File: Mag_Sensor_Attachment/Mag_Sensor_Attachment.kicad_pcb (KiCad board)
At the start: 2 copper layers, 14 x 15.8 mm, 5 parts, among them J2 Conn_01x06_Socket, U1 MA730

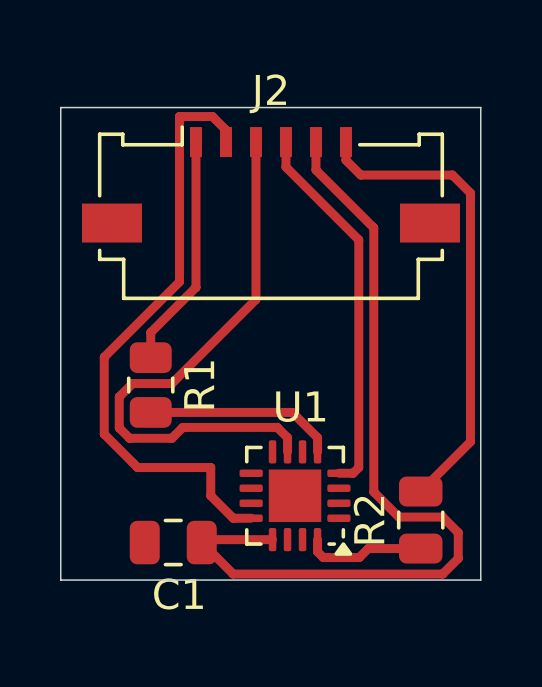
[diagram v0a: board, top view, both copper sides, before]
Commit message: added to schematic
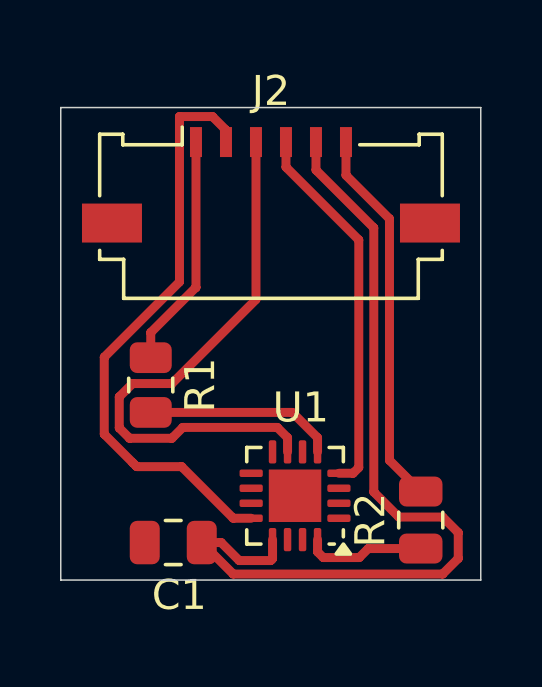
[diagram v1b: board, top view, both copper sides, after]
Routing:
- net /Mag_High: track 15.8 -> 12.7 mm
- net /VDD: track 28.3 -> 29.2 mm
- net /MAG_CLK: track 20.4 -> 19.8 mm
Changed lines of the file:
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@@
 	)
 	(segment
-		(start 149.56 99.4025)
-		(end 147.2975 99.4025)
+		(start 147.8475 99.5)
+		(end 147.2 99.5)
 		(width 0.3)
 		(layer "F.Cu")
@@
 	)
 	(segment
+		(start 149.56 99.4025)
+		(end 149.56 100.04)
+		(width 0.3)
+		(layer "F.Cu")
+		(net 2)
+	)
+	(segment
 		(start 152.934772 89.009772)
 		(end 152.934772 97.815228)
@@
 	)
 	(segment
+		(start 149.5 100.1)
+		(end 148.4475 100.1)
+		(width 0.3)
+		(layer "F.Cu")
+		(net 2)
+	)
+	(segment
+		(start 149.56 100.04)
+		(end 149.5 100.1)
+		(width 0.3)
+		(layer "F.Cu")
+		(net 2)
+	)
+	(segment
 		(start 148.25 100.55)
 		(end 147.2 99.5)
@@
 	)
 	(segment
-		(start 147.2975 99.4025)
-		(end 147.2 99.5)
+		(start 148.4475 100.1)
+		(end 147.8475 99.5)
 		(width 0.3)
 		(layer "F.Cu")
@@
 	)
 	(segment
+		(start 146.4575 90.812044)
+		(end 146.4575 85.3)
+		(width 0.3)
+		(layer "F.Cu")
+		(net 6)
+	)
+	(segment
+		(start 145.031218 96.968782)
+		(end 144.906218 96.843782)
+		(width 0.3)
+		(layer "F.Cu")
+		(net 6)
+	)
+	(segment
+		(start 143.95 93.319544)
+		(end 146.4575 90.812044)
+		(width 0.3)
+		(layer "F.Cu")
+		(net 6)
+	)
+	(segment
+		(start 148.25 98.69)
+		(end 146.528782 96.968782)
+		(width 0.3)
+		(layer "F.Cu")
+		(net 6)
+	)
+	(segment
+		(start 144.906218 96.843782)
+		(end 143.95 95.887563)
+		(width 0.3)
+		(layer "F.Cu")
+		(net 6)
+	)
+	(segment
+		(start 147.5575 85.3)
+		(end 148.0075 85.75)
+		(width 0.3)
+		(layer "F.Cu")
+		(net 6)
+	)
+	(segment
+		(start 148.0075 85.75)
+		(end 148.0075 86.15)
+		(width 0.3)
+		(layer "F.Cu")
+		(net 6)
+	)
+	(segment
+		(start 146.528782 96.968782)
+		(end 145.031218 96.968782)
+		(width 0.3)
+		(layer "F.Cu")
+		(net 6)
+	)
+	(segment
 		(start 143.95 95.887563)
-		(end 144.906218 96.843782)
-		(width 0.3)
-		(layer "F.Cu")
-		(net 6)
-	)
-	(segment
-		(start 148.0075 86.15)
-		(end 148.0075 85.75)
-		(width 0.3)
-		(layer "F.Cu")
-		(net 6)
-	)
-	(segment
-		(start 147.5575 85.3)
-		(end 146.4575 85.3)
-		(width 0.3)
-		(layer "F.Cu")
-		(net 6)
-	)
-	(segment
-		(start 143.95 93.319544)
-		(end 143.95 95.887563)
-		(width 0.3)
-		(layer "F.Cu")
-		(net 6)
-	)
-	(segment
-		(start 148.25 98.69)
-		(end 147.5 97.94)
-		(width 0.3)
-		(layer "F.Cu")
-		(net 6)
-	)
-	(segment
-		(start 146.4575 90.812044)
 		(end 143.95 93.319544)
 		(width 0.3)
@@
 	(segment
 		(start 146.4575 85.3)
-		(end 146.4575 90.812044)
-		(width 0.3)
-		(layer "F.Cu")
-		(net 6)
-	)
-	(segment
-		(start 148.0075 85.75)
 		(end 147.5575 85.3)
 		(width 0.3)
@@
 	)
 	(segment
-		(start 147.5 97)
-		(end 145.062436 97)
-		(width 0.3)
-		(layer "F.Cu")
-		(net 6)
-	)
-	(segment
-		(start 148.25 98.69)
-		(end 148.8475 98.69)
-		(width 0.3)
-		(layer "F.Cu")
-		(net 6)
-	)
-	(segment
-		(start 147.5 97.94)
-		(end 147.5 97)
-		(width 0.3)
-		(layer "F.Cu")
-		(net 6)
-	)
-	(segment
-		(start 145.062436 97)
-		(end 144.906218 96.843782)
-		(width 0.3)
-		(layer "F.Cu")
-		(net 6)
-	)
-	(segment
-		(start 156.1575 87.85)
-		(end 156.1575 96.1425)
+		(start 148.8475 98.69)
+		(end 148.25 98.69)
+		(width 0.3)
+		(layer "F.Cu")
+		(net 6)
+	)
+	(segment
+		(start 152.0075 87.2575)
+		(end 152.0075 86.15)
 		(width 0.3)
 		(layer "F.Cu")
@@
 	)
 	(segment
-		(start 156.1575 96.1425)
-		(end 154.5 97.8)
+		(start 153.4575 88.7075)
+		(end 152.0075 87.2575)
 		(width 0.3)
 		(layer "F.Cu")
@@
 	)
 	(segment
-		(start 155.5575 87.25)
-		(end 156.1575 87.85)
+		(start 153.4575 96.7575)
+		(end 153.4575 88.7075)
 		(width 0.3)
 		(layer "F.Cu")
@@
 	)
 	(segment
-		(start 152.5 87.25)
-		(end 155.5575 87.25)
-		(width 0.3)
-		(layer "F.Cu")
-		(net 7)
-	)
-	(segment
-		(start 152.0075 86.15)
-		(end 152.0075 86.7575)
-		(width 0.3)
-		(layer "F.Cu")
-		(net 7)
-	)
-	(segment
-		(start 152.0075 86.7575)
-		(end 152.5 87.25)
-		(width 0.3)
-		(layer "F.Cu")
+		(start 154.5 97.8)
+		(end 153.4575 96.7575)
+		(width 0.3)
+		(layer "F.Cu")

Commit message: Check up
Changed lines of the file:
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@@
 		(start 152.434772 89.412272)
 		(end 150.0075 86.985)
-		(width 0.3)
+		(width 0.15)
 		(layer "F.Cu")
 		(net 3)
@@
 		(start 152.244772 97.19)
 		(end 152.434772 97)
-		(width 0.3)
+		(width 0.15)
 		(layer "F.Cu")
 		(net 3)
@@
 		(start 150.0075 86.985)
 		(end 150.0075 86.15)
-		(width 0.3)
+		(width 0.15)
 		(layer "F.Cu")
 		(net 3)
@@
 		(start 151.7725 97.19)
 		(end 152.244772 97.19)
-		(width 0.3)
+		(width 0.15)
 		(layer "F.Cu")
 		(net 3)
@@
 		(start 152.434772 97)
 		(end 152.434772 89.412272)
-		(width 0.3)
-		(layer "F.Cu")
-		(net 3)
-	)
-	(segment
-		(start 146.567956 95.6625)
+		(width 0.15)
+		(layer "F.Cu")
+		(net 3)
+	)
+	(segment
+		(start 144.894544 94.2)
+		(end 146.205456 94.2)
+		(width 0.15)
+		(layer "F.Cu")
+		(net 4)
+	)
+	(segment
+		(start 146.205456 96.025)
+		(end 144.794544 96.025)
+		(width 0.15)
+		(layer "F.Cu")
+		(net 4)
+	)
+	(segment
+		(start 150.06 96.4775)
+		(end 150.06 95.5725)
+		(width 0.15)
+		(layer "F.Cu")
+		(net 4)
+	)
+	(segment
+		(start 146.717956 95.5125)
 		(end 146.205456 96.025)
-		(width 0.3)
+		(width 0.15)
+		(layer "F.Cu")
+		(net 4)
+	)
+	(segment
+		(start 144.794544 96.025)
+		(end 144.45 95.680456)
+		(width 0.15)
 		(layer "F.Cu")
 		(net 4)
@@
 		(start 144.45 95.680456)
 		(end 144.45 94.644544)
-		(width 0.3)
-		(layer "F.Cu")
-		(net 4)
-	)
-	(segment
-		(start 146.205456 96.025)
-		(end 144.794544 96.025)
-		(width 0.3)
-		(layer "F.Cu")
-		(net 4)
-	)
-	(segment
-		(start 144.894544 94.2)
-		(end 146.205456 94.2)
-		(width 0.3)
+		(width 0.15)
+		(layer "F.Cu")
+		(net 4)
+	)
+	(segment
+		(start 150 95.5125)
+		(end 146.717956 95.5125)
+		(width 0.15)
+		(layer "F.Cu")
+		(net 4)
+	)
+	(segment
+		(start 149.0075 91.397956)
+		(end 149.0075 86.15)
+		(width 0.15)
+		(layer "F.Cu")
+		(net 4)
+	)
+	(segment
+		(start 144.45 94.644544)
+		(end 144.894544 94.2)
+		(width 0.15)
 		(layer "F.Cu")
 		(net 4)
@@
 		(start 146.205456 94.2)
 		(end 149.0075 91.397956)
-		(width 0.3)
-		(layer "F.Cu")
-		(net 4)
-	)
-	(segment
-		(start 149.717596 95.6625)
-		(end 146.567956 95.6625)
-		(width 0.3)
-		(layer "F.Cu")
-		(net 4)
-	)
-	(segment
-		(start 144.794544 96.025)
-		(end 144.45 95.680456)
-		(width 0.3)
-		(layer "F.Cu")
-		(net 4)
-	)
-	(segment
-		(start 149.0075 91.397956)
-		(end 149.0075 86.15)
-		(width 0.3)
-		(layer "F.Cu")
-		(net 4)
-	)
-	(segment
-		(start 150.06 96.4775)
-		(end 150.06 96.004904)
-		(width 0.3)
-		(layer "F.Cu")
-		(net 4)
-	)
-	(segment
-		(start 150.06 96.004904)
-		(end 149.717596 95.6625)
-		(width 0.3)
-		(layer "F.Cu")
-		(net 4)
-	)
-	(segment
-		(start 144.45 94.644544)
-		(end 144.894544 94.2)
-		(width 0.3)
+		(width 0.15)
+		(layer "F.Cu")
+		(net 4)
+	)
+	(segment
+		(start 150.06 95.5725)
+		(end 150 95.5125)
+		(width 0.15)
 		(layer "F.Cu")
 		(net 4)
@@
 		(start 147 91)
 		(end 147.0075 91)
-		(width 0.3)
+		(width 0.15)
 		(layer "F.Cu")
 		(net 5)
@@
 		(start 145.5 92.5)
 		(end 147 91)
-		(width 0.3)
+		(width 0.15)
 		(layer "F.Cu")
 		(net 5)
@@
 		(start 147.0075 91)
 		(end 147.0075 86.15)
-		(width 0.3)
+		(width 0.15)
 		(layer "F.Cu")
 		(net 5)
@@
 		(start 145.5 93.3375)
 		(end 145.5 92.5)
-		(width 0.3)
+		(width 0.15)
 		(layer "F.Cu")
 		(net 5)
@@
 		(start 146.4575 90.812044)
 		(end 146.4575 85.3)
-		(width 0.3)
+		(width 0.15)
 		(layer "F.Cu")
 		(net 6)
@@
 		(start 145.031218 96.968782)
 		(end 144.906218 96.843782)
-		(width 0.3)
+		(width 0.15)
 		(layer "F.Cu")
 		(net 6)
@@
 		(start 143.95 93.319544)
 		(end 146.4575 90.812044)
-		(width 0.3)
+		(width 0.15)
 		(layer "F.Cu")
 		(net 6)
@@
 		(start 148.25 98.69)
 		(end 146.528782 96.968782)
-		(width 0.3)
+		(width 0.15)
 		(layer "F.Cu")
 		(net 6)
@@
 		(start 144.906218 96.843782)
 		(end 143.95 95.887563)
-		(width 0.3)
+		(width 0.15)
 		(layer "F.Cu")
 		(net 6)
@@
 		(start 147.5575 85.3)
 		(end 148.0075 85.75)
-		(width 0.3)
+		(width 0.15)
 		(layer "F.Cu")
 		(net 6)
@@
 		(start 148.0075 85.75)
 		(end 148.0075 86.15)
-		(width 0.3)
+		(width 0.15)
 		(layer "F.Cu")
 		(net 6)
@@
 		(start 146.528782 96.968782)
 		(end 145.031218 96.968782)
-		(width 0.3)
+		(width 0.15)
 		(layer "F.Cu")
 		(net 6)
@@
 		(start 143.95 95.887563)
 		(end 143.95 93.319544)
-		(width 0.3)
+		(width 0.15)
 		(layer "F.Cu")
 		(net 6)
@@
 		(start 146.4575 85.3)
 		(end 147.5575 85.3)
-		(width 0.3)
+		(width 0.15)
 		(layer "F.Cu")
 		(net 6)
@@
 		(start 148.8475 98.69)
 		(end 148.25 98.69)
-		(width 0.3)
+		(width 0.15)
 		(layer "F.Cu")
 		(net 6)
@@
 		(start 152.0075 87.2575)
 		(end 152.0075 86.15)
-		(width 0.3)
+		(width 0.15)
 		(layer "F.Cu")
 		(net 7)
@@
 		(start 153.4575 88.7075)
 		(end 152.0075 87.2575)
-		(width 0.3)
-		(layer "F.Cu")
-		(net 7)
-	)
-	(segment
-		(start 153.4575 96.7575)
+		(width 0.15)
+		(layer "F.Cu")
+		(net 7)
+	)
+	(segment
+		(start 154.475 96.5175)
+		(end 153.4575 95.5)
+		(width 0.15)
+		(layer "F.Cu")
+		(net 7)
+	)
+	(segment
+		(start 154.475 97.775)
+		(end 154.475 96.5175)
+		(width 0.15)
+		(layer "F.Cu")
+		(net 7)
+	)
+	(segment
+		(start 153.4575 95.5)
 		(end 153.4575 88.7075)
-		(width 0.3)
+		(width 0.15)
 		(layer "F.Cu")
 		(net 7)
@@
 	(segment
 		(start 154.5 97.8)
-		(end 153.4575 96.7575)
-		(width 0.3)
+		(end 154.475 97.775)
+		(width 0.15)
 		(layer "F.Cu")
 		(net 7)
@@
 		(start 151.06 96.004904)
 		(end 151.06 96.4775)
-		(width 0.3)
+		(width 0.15)
 		(layer "F.Cu")
 		(net 8)
@@
 		(start 150.217596 95.1625)
 		(end 151.06 96.004904)
-		(width 0.3)
+		(width 0.15)
 		(layer "F.Cu")
 		(net 8)
@@
 		(start 145.5 95.1625)
 		(end 150.217596 95.1625)
-		(width 0.3)
+		(width 0.15)
 		(layer "F.Cu")
 		(net 8)
@@
 		(start 152.75 99.7)
 		(end 154.5 99.7)
-		(width 0.3)
+		(width 0.15)
 		(layer "F.Cu")
 		(net 9)
@@
 		(start 151.06 99.81)
 		(end 151.25 100)
-		(width 0.3)
+		(width 0.15)
 		(layer "F.Cu")
 		(net 9)
@@
 		(start 151.06 99.4025)
 		(end 151.06 99.81)
-		(width 0.3)
+		(width 0.15)
 		(layer "F.Cu")
 		(net 9)
@@
 		(start 151.25 100)
 		(end 152.45 100)
-		(width 0.3)
+		(width 0.15)
 		(layer "F.Cu")
 		(net 9)
@@
 		(start 152.45 100)
 		(end 152.75 99.7)
-		(width 0.3)
-		(layer "F.Cu")
-		(net 9)
+		(width 0.15)
+		(layer "F.Cu")
+		(net 9)

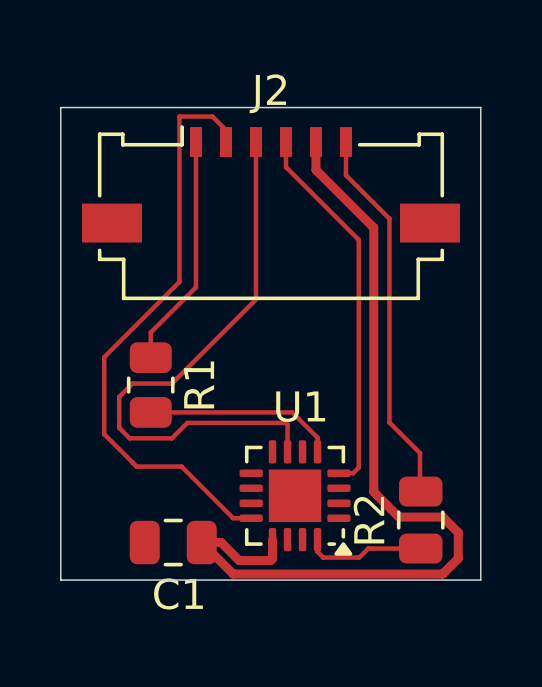
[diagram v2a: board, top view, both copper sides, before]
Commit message: rerouted VDD
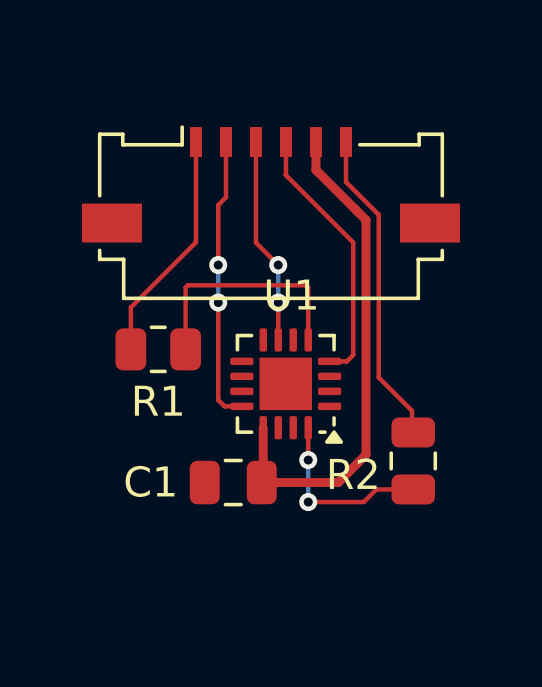
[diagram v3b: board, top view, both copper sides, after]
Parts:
- moved U1 3.74 mm to (150.0, 94.2)
- moved C1 2.83 mm to (148.2, 97.5)
- moved R2 1.99 mm to (154.2, 96.8)
- moved R1 1.22 mm to (145.8, 93.1), turned to 0 degrees
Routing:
- net /VDD: track 29.2 -> 16.8 mm
- net /MAGSLV_Output: track 19.1 -> 6.91 mm, vias 0 -> 2
- net /MAG_CLK: track 19.8 -> 9.58 mm, vias 0 -> 2
- net /MGSLV_Input: track 12.6 -> 8.91 mm
- net Net-(U1-MGH): track 4.05 -> 6.15 mm, vias 0 -> 2
- net /Mag_High: track 12.7 -> 10.6 mm
- net Net-(U1-~{CS}): track 6.38 -> 7.96 mm
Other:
- board outline removed

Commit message: random stitching vias
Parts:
- added D1: LED, LED_SMD:LED_0805_2012Metric, F.Cu at (144.5, 97.5)
- added R3: 1k, Resistor_SMD:R_0805_2012Metric, F.Cu at (145.8, 95.4)
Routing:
- net /VDD: track 16.8 -> 19.5 mm
- net Net-(D1-A): track 0.00 -> 2.59 mm
- net (no net): vias 0 -> 7

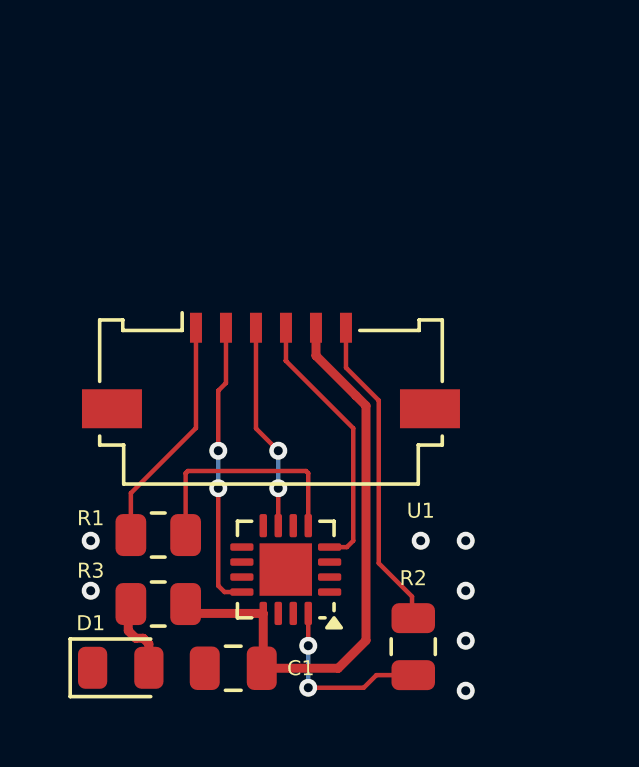
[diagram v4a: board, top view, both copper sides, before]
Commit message: (label "LDO_1.8V" (at 124.46 142.24 0) (fields_auteplaced yes)   (effects (font (size 0.762 0.762)) (justify left bottom)) (uuid "5df45f02-f0ff-424b-b1b0-8f9540b4e896") ) (label "LDO_1.8V" (at 124.46 142.24 0) (fields_autoplaced yes)   (effects (font (size 0.762 0.762)) (justify left bottom)) (uuid "5df45f02-f0ff-424b-b1b0-8f9540b4e896") )
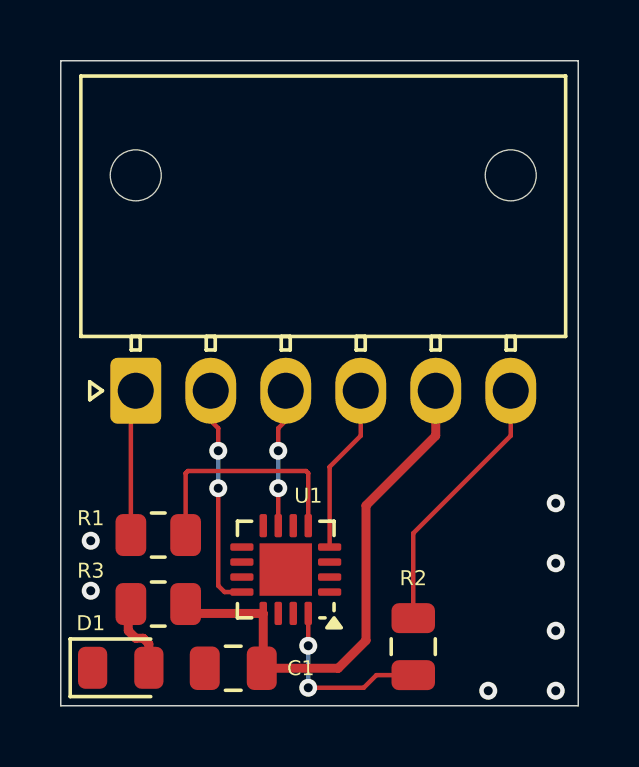
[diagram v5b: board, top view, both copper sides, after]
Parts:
- J2: footprint Connector_FFC-FPC:Molex_200528-0060_1x06-1MP_P1.00mm_Horizontal -> Connector_Molex:Molex_Nano-Fit_105313-xx06_1x06_P2.50mm_Horizontal
- moved J2 4.66 mm to (145.0, 88.2), turned to 90 degrees
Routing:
- net /MGSLV_Input: track 8.91 -> 6.00 mm
- net /MAG_CS: track 7.81 -> 5.24 mm
- net /MAGSLV_Output: track 6.91 -> 4.96 mm
- net /MAG_CLK: track 9.58 -> 7.84 mm
- net /VDD: track 19.5 -> 18.1 mm
- net /Mag_High: track 10.6 -> 9.29 mm
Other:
- board outline added: 17.2 x 21.5 mm

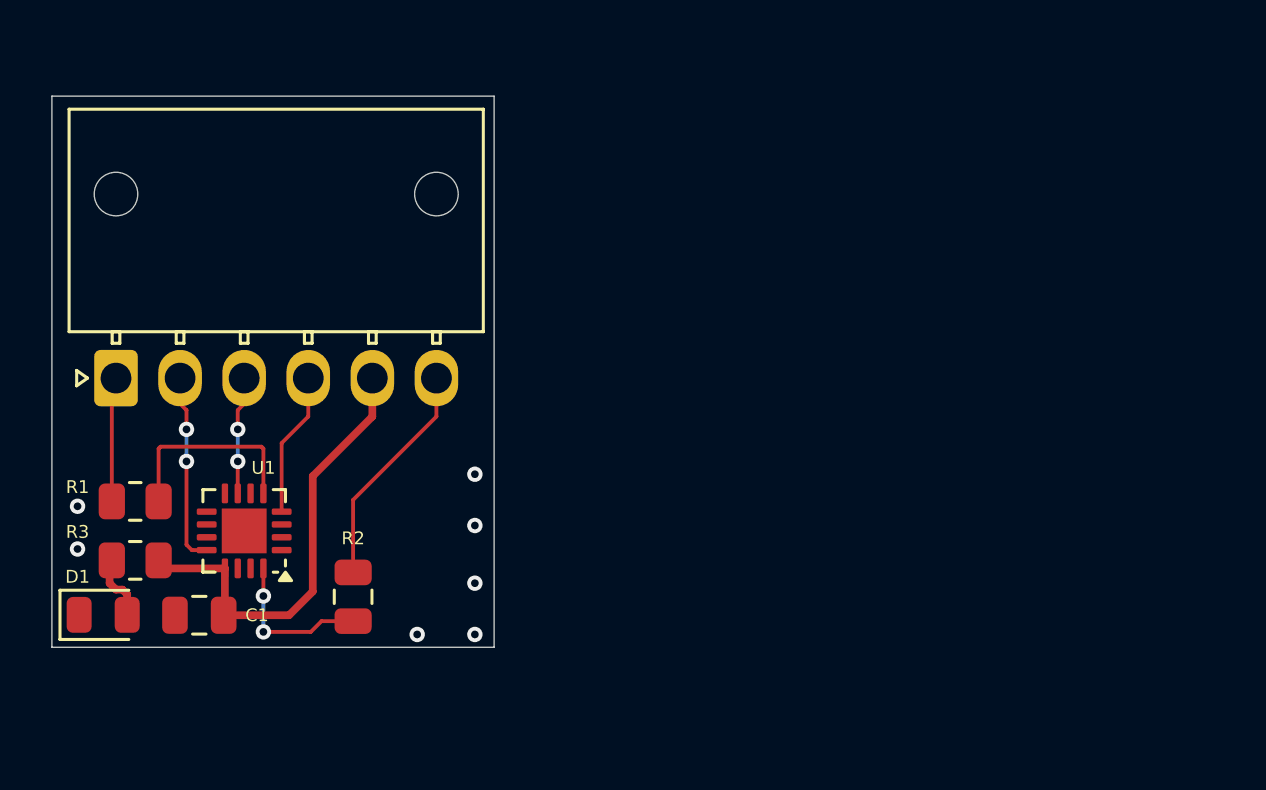
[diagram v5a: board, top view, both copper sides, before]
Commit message: Made Mag compact
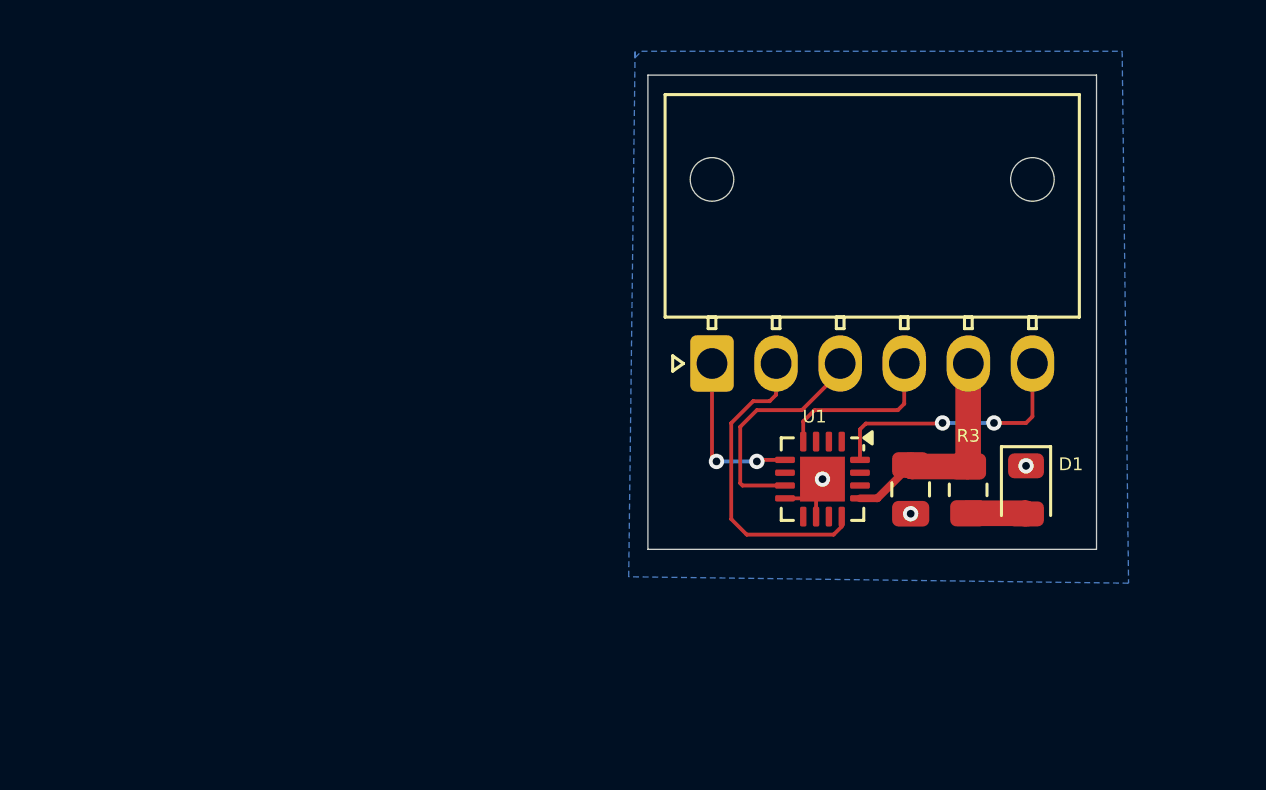
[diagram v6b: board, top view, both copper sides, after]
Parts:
- removed R1: 66k, Resistor_SMD:R_0805_2012Metric
- removed R2: 66k, Capacitor_SMD:C_0805_2012Metric
- moved D1 36.3 mm to (180.5, 92.6), turned to -90 degrees
- moved R3 32.6 mm to (178.2, 92.6), turned to -90 degrees
- moved C1 28.2 mm to (176.0, 92.6), turned to 90 degrees
- moved J2 23.3 mm to (168.2, 87.7)
- moved U1 22.7 mm to (172.6, 92.2), turned to -90 degrees
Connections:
- U1 pad 16: Net-(U1-MGH) -> /Mag_High
- U1 pad 5: Net-(U1-~{CS}) -> /MAG_CS
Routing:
- net /VDD: track 18.1 -> 8.80 mm
- net Net-(U1-~{CS}): track 7.96 -> 0.00 mm
- net Net-(U1-MGH): track 6.15 -> 0.00 mm, vias 2 -> 0
- net /MAG_CLK: track 7.84 -> 12.3 mm, vias 2 -> 0
- net /MAGSLV_Output: track 4.96 -> 9.10 mm, vias 2 -> 0
- net GND: track 0.00 -> 3.34 mm, vias 0 -> 3
- net /MAG_CS: track 5.24 -> 6.82 mm, vias 0 -> 2
- net /Mag_High: track 9.29 -> 10.2 mm, vias 0 -> 2
- net /MGSLV_Input: track 6.00 -> 6.58 mm
- net (no net): vias 7 -> 0
- added copper zone on B.Cu, net GND
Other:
- board size 17.2 x 21.5 mm -> 17.5 x 18.5 mm
